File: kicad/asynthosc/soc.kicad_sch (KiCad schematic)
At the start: 50 parts, among them J15 Conn_02x04_Odd_Even, J3 Conn_ARM_SWD_TagConnect_TC203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, J4 Conn_02x07_Odd_Even, J5 Conn_02x04_Odd_Even, SW1 SW_Push, U6 STM32F723VETx, U7 W25Q32JVSS, Y1 8MHz, 8pF

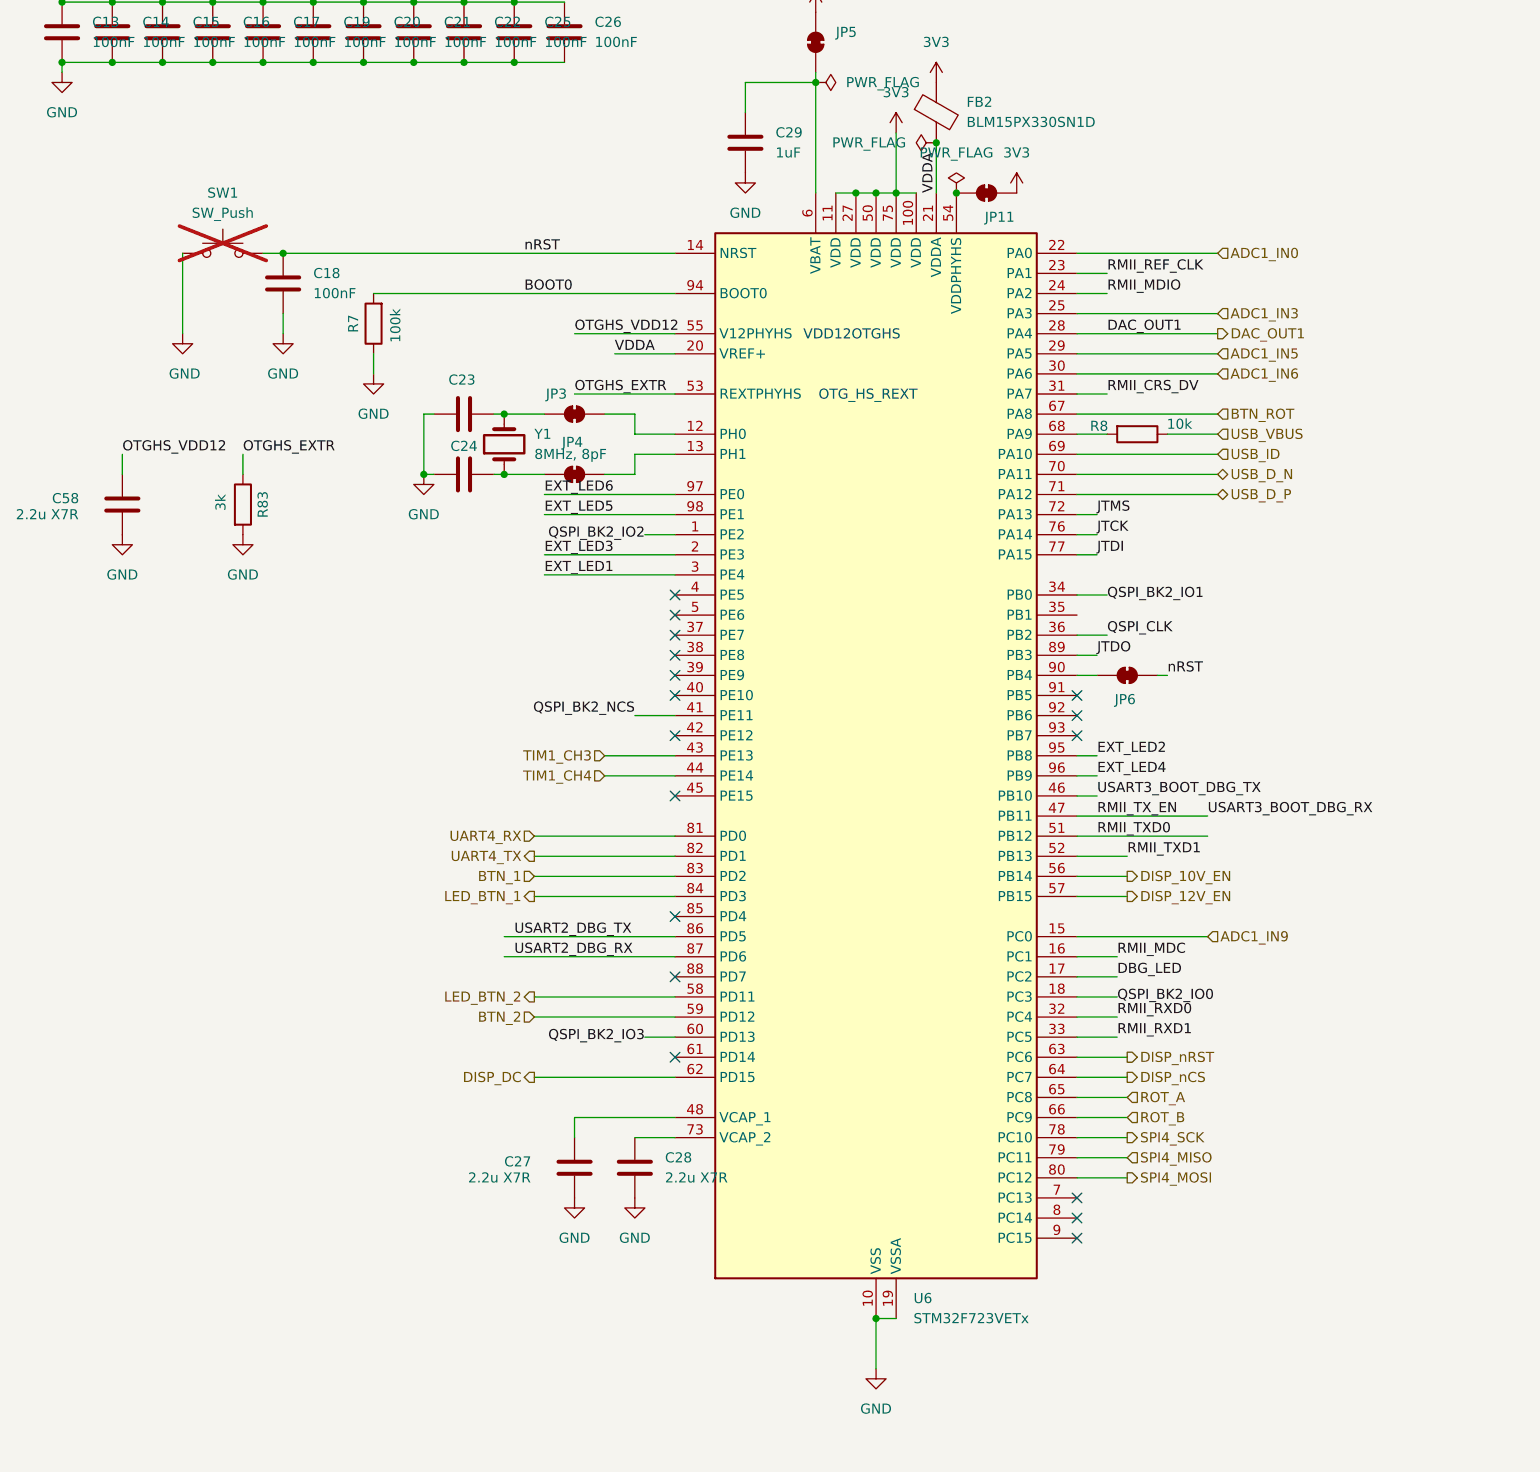
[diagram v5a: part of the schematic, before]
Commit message: sch: change stm32 ref for adc
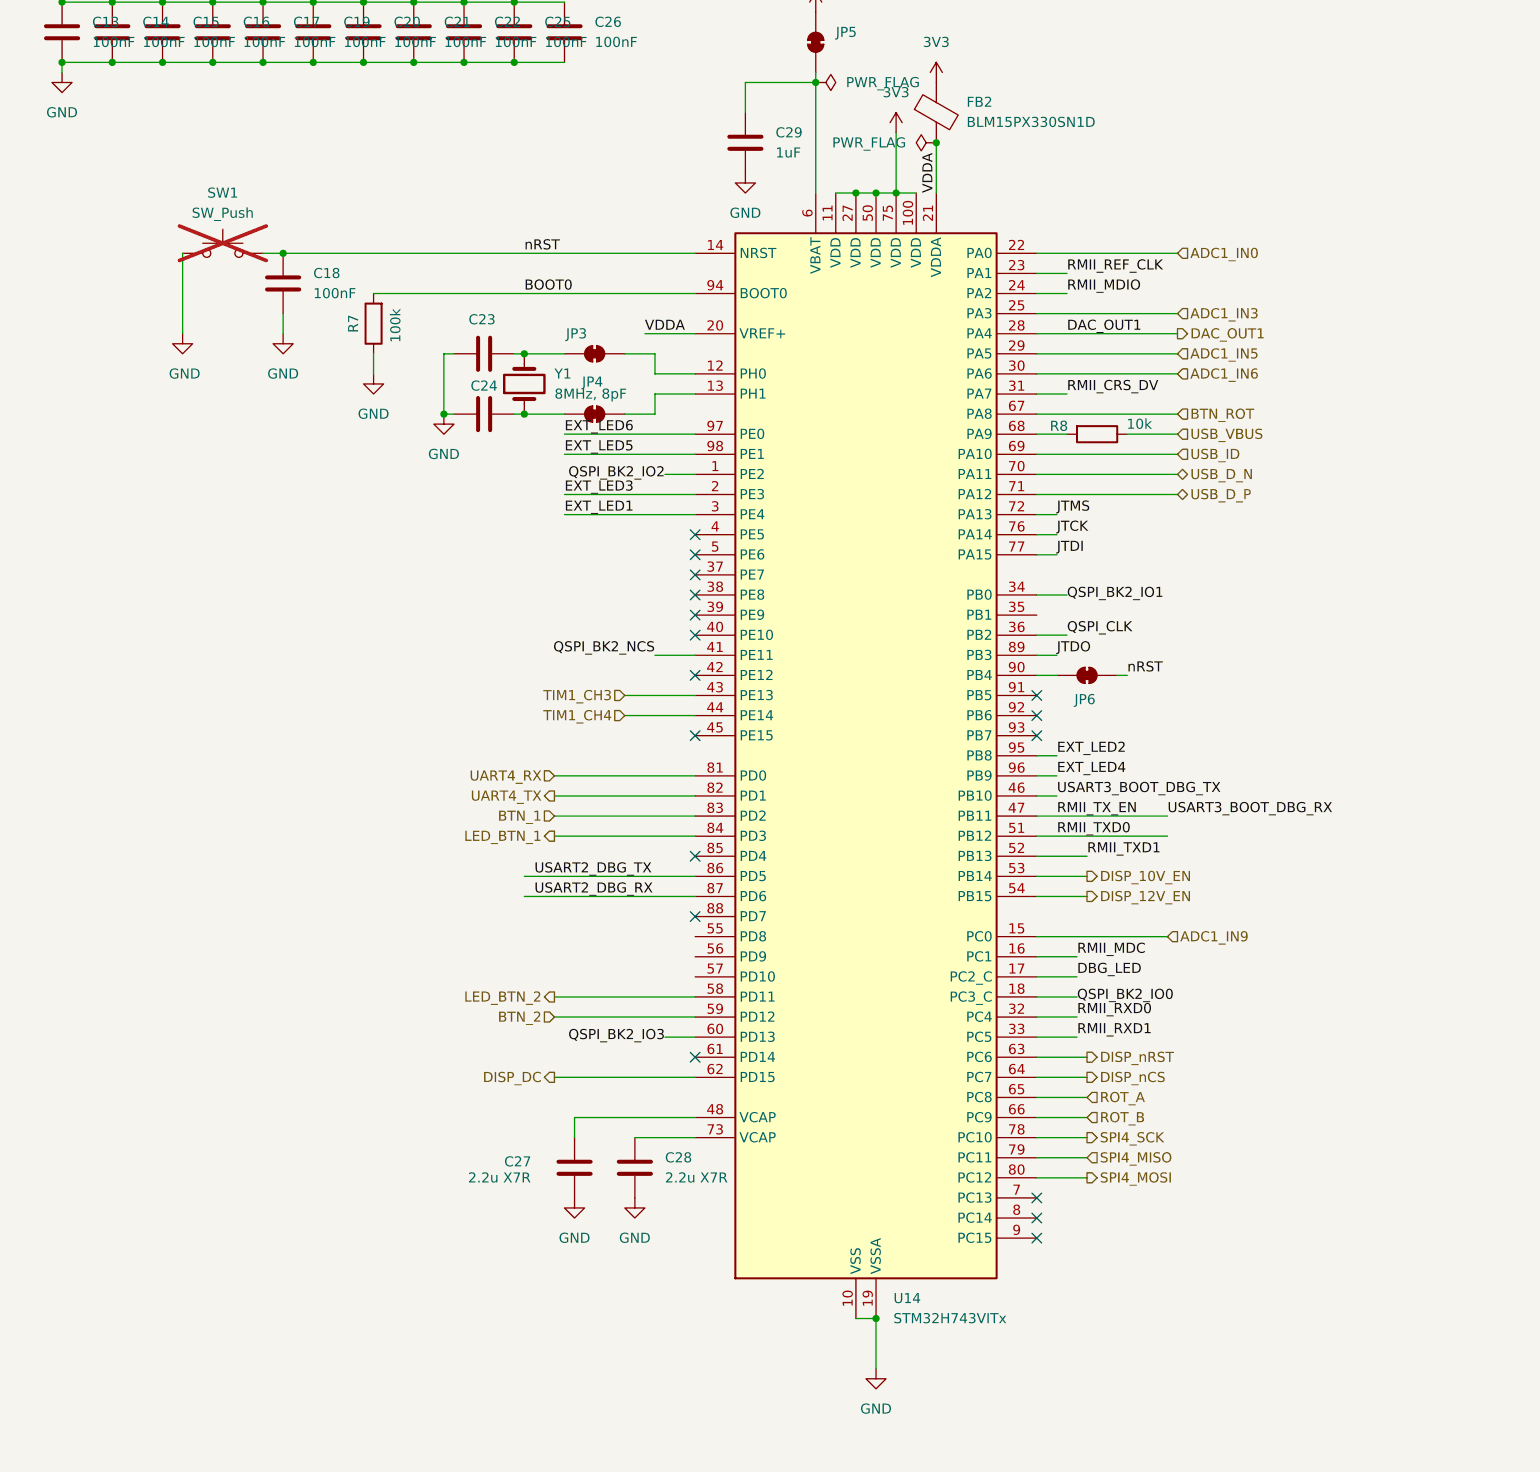
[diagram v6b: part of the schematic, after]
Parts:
- removed C58: 2.2u X7R, Capacitor_SMD:C_0402_1005Metric, symbol Device:C
- removed JP11: SolderJumper_2_Bridged, asynthosc:SolderJumper_0402_1005Metric_Bridged, symbol Jumper:SolderJumper_2_Bridged
- removed R83: 3k, Resistor_SMD:R_0402_1005Metric, symbol Device:R
- removed U6: STM32F723VETx, Package_QFP:LQFP-100_14x14mm_P0.5mm, symbol MCU_ST_STM32F7:STM32F723VETx
- added U14: STM32H743VITx, Package_QFP:LQFP-100_14x14mm_P0.5mm, symbol MCU_ST_STM32H7:STM32H743VITx
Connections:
- net 3V3: now also U14.100 (VDD), U14.11 (VDD), U14.27 (VDD), U14.50 (VDD), U14.75 (VDD)
- net ADC1_IN0: now also U14.22 (PA0)
- net ADC1_IN3: now also U14.25 (PA3)
- net ADC1_IN5: now also U14.29 (PA5)
- net ADC1_IN6: now also U14.30 (PA6)
- net ADC1_IN9: now also U14.15 (PC0)
- net BOOT0: now also U14.94 (BOOT0)
- net BTN_1: now also U14.83 (PD2)
- net BTN_2: now also U14.59 (PD12)
- net BTN_ROT: now also U14.67 (PA8)
- net DAC_OUT1: now also U14.28 (PA4)
- net DBG_LED: now also U14.17 (PC2_C)
- net DISP_10V_EN: now also U14.53 (PB14)
- net DISP_12V_EN: now also U14.54 (PB15)
- net DISP_DC: now also U14.62 (PD15)
- net DISP_nCS: now also U14.64 (PC7)
- net DISP_nRST: now also U14.63 (PC6)
- net EXT_LED1: now also U14.3 (PE4)
- net EXT_LED2: now also U14.95 (PB8)
- net EXT_LED3: now also U14.2 (PE3)
- net EXT_LED4: now also U14.96 (PB9)
- net EXT_LED5: now also U14.98 (PE1)
- net EXT_LED6: now also U14.97 (PE0)
- net GND: now also U14.10 (VSS), U14.19 (VSSA), U14.26 (VSS), U14.49 (VSS), U14.74 (VSS), U14.99 (VSS)
- net JTCK: now also U14.76 (PA14)
- net JTDI: now also U14.77 (PA15)
- net JTDO: now also U14.89 (PB3)
- net JTMS: now also U14.72 (PA13)
- net LED_BTN_1: now also U14.84 (PD3)
- net LED_BTN_2: now also U14.58 (PD11)
- net QSPI_BK2_IO0: now also U14.18 (PC3_C)
- net QSPI_BK2_IO1: now also U14.34 (PB0)
- net QSPI_BK2_IO2: now also U14.1 (PE2)
- net QSPI_BK2_IO3: now also U14.60 (PD13)
- net QSPI_BK2_NCS: now also U14.41 (PE11)
- net QSPI_CLK: now also U14.36 (PB2)
- net RMII_CRS_DV: now also U14.31 (PA7)
- net RMII_MDC: now also U14.16 (PC1)
- net RMII_MDIO: now also U14.24 (PA2)
- net RMII_REF_CLK: now also U14.23 (PA1)
- net RMII_RXD0: now also U14.32 (PC4)
- net RMII_RXD1: now also U14.33 (PC5)
- net RMII_TXD0: now also U14.51 (PB12)
- net RMII_TXD1: now also U14.52 (PB13)
- net RMII_TX_EN: now also U14.47 (PB11)
- net ROT_A: now also U14.65 (PC8)
- net ROT_B: now also U14.66 (PC9)
- net SPI4_MISO: now also U14.79 (PC11)
- net SPI4_MOSI: now also U14.80 (PC12)
- net SPI4_SCK: now also U14.78 (PC10)
- net TIM1_CH3: now also U14.43 (PE13)
- net TIM1_CH4: now also U14.44 (PE14)
- net UART4_RX: now also U14.81 (PD0)
- net UART4_TX: now also U14.82 (PD1)
- net USART2_DBG_RX: now also U14.87 (PD6)
- net USART2_DBG_TX: now also U14.86 (PD5)
- net USART3_BOOT_DBG_TX: now also U14.46 (PB10)
- net USB_D_N: now also U14.70 (PA11)
- net USB_D_P: now also U14.71 (PA12)
- net USB_ID: now also U14.69 (PA10)
- net VDDA: now also U14.20 (VREF+), U14.21 (VDDA)
- net nRST: now also U14.14 (NRST)
- net at JP4.1 (A): now also U14.13 (PH1)
- net at JP3.1 (A): now also U14.12 (PH0)
- net at C29.1, JP5.1 (A): now also U14.6 (VBAT)
- net at C27.1: now also U14.48 (VCAP)
- net at R8.2: now also U14.68 (PA9)
- net at C28.1: now also U14.73 (VCAP)
- net at JP6.2 (B): now also U14.90 (PB4)
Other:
- note removed: "OTG_HS_REXT"
- note removed: "VDD12OTGHS"
- moved on the sheet: C23, C24, JP3, JP4, JP6, R8, Y1

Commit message: bom: update mfr, serials and lcsc fields
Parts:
- FB2: LCSC (none) -> C160974
- J15, J5: LCSC (none) -> C192300; Manufacturer (none) -> Boomele; RefNum _na_ -> 2.54-2*4P
- J4: LCSC (none) -> C84004; Manufacturer (none) -> Boomele; RefNum _na_ -> 2.54-2*7P
- SW1: LCSC (none) -> C5127964; Manufacturer Boomele -> Boomele
- U14: LCSC (none) -> C114409; Manufacturer (none) -> STMicroelectronics; RefNum (none) -> STM32H743VITx
- U7: LCSC (none) -> C179173
- Y1: LCSC (none) -> C889706
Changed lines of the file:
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@@
 			)
 		)
-		(property "LCSC" ""
+		(property "LCSC" "C192300 "
 			(at 328.93 166.37 0)
 			(effects
@@
 			)
 		)
-		(property "Manufacturer" ""
+		(property "Manufacturer" "Boomele "
 			(at 328.93 166.37 0)
 			(effects
@@
 			)
 		)
-		(property "RefNum" "_na_"
+		(property "RefNum" "2.54-2*4P"
 			(at 328.93 166.37 0)
 			(effects
@@
 			)
 		)
-		(property "LCSC" ""
+		(property "LCSC" "C84004 "
 			(at 326.39 86.36 0)
 			(effects
@@
 			)
 		)
-		(property "Manufacturer" ""
+		(property "Manufacturer" "Boomele "
 			(at 326.39 86.36 0)
 			(effects
@@
 			)
 		)
-		(property "RefNum" "_na_"
+		(property "RefNum" "2.54-2*7P"
 			(at 326.39 86.36 0)
 			(effects
@@
 			)
 		)
-		(property "LCSC" ""
+		(property "LCSC" "C192300 "
 			(at 328.93 134.62 0)
 			(effects
@@
 			)
 		)
-		(property "Manufacturer" ""
+		(property "Manufacturer" "Boomele "
 			(at 328.93 134.62 0)
 			(effects
@@
 			)
 		)
-		(property "RefNum" "_na_"
+		(property "RefNum" "2.54-2*4P"
 			(at 328.93 134.62 0)
 			(effects
@@
 			)
 		)
-		(property "LCSC" ""
+		(property "LCSC" "C179173"
 			(at 278.13 218.44 0)
 			(effects
@@
 			)
 		)
+		(property "LCSC" " C114409"
+			(at 124.46 115.57 0)
+			(effects
+				(font
+					(size 1.27 1.27)
+				)
+				(hide yes)
+			)
+		)
+		(property "Manufacturer" "STMicroelectronics"
+			(at 124.46 115.57 0)
+			(effects
+				(font
+					(size 1.27 1.27)
+				)
+				(hide yes)
+			)
+		)
+		(property "RefNum" "STM32H743VITx"
+			(at 124.46 115.57 0)
+			(effects
+				(font
+					(size 1.27 1.27)
+				)
+				(hide yes)
+			)
+		)
 		(pin "86"
 		)
@@
 			)
 		)
-		(property "LCSC" ""
+		(property "LCSC" "C889706"
 			(at 82.55 68.58 0)
 			(effects
@@
 			)
 		)
-		(property "LCSC" ""
+		(property "LCSC" "C160974"
 			(at 134.62 34.29 0)
 			(effects
@@
 			)
 		)
-		(property "LCSC" ""
+		(property "LCSC" "C5127964"
 			(at 44.45 52.07 0)
 			(effects
@@
 			)
 		)
-		(property "Manufacturer" " Boomele"
+		(property "Manufacturer" "Boomele"
 			(at 44.45 52.07 0)
 			(effects

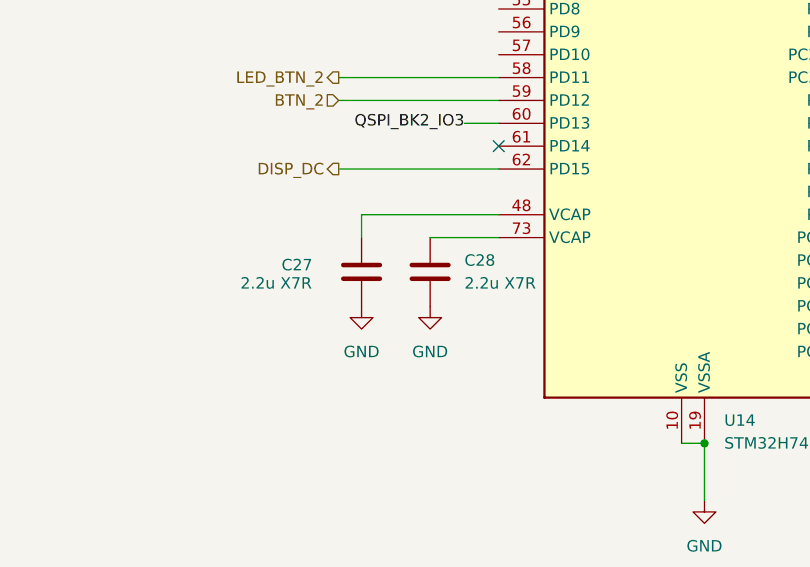
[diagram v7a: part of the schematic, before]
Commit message: bom: update for better bom
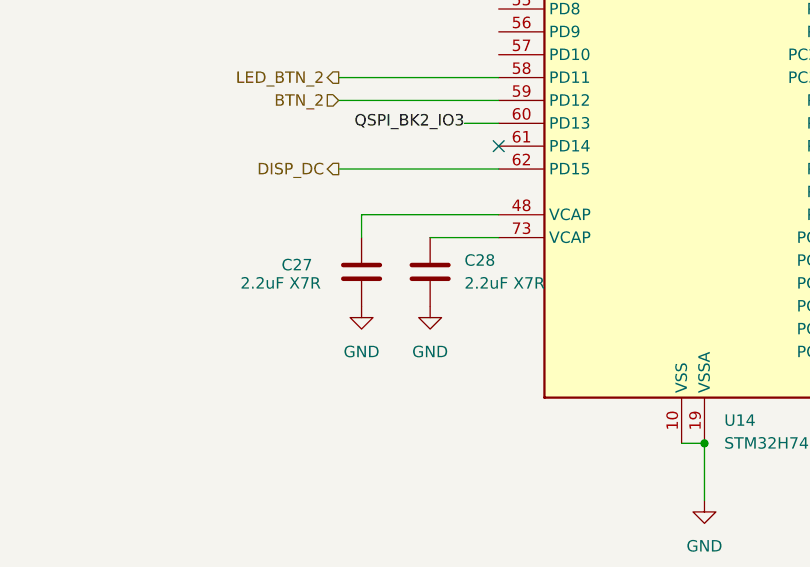
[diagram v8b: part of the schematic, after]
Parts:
- C27, C28: value 2.2u X7R -> 2.2uF X7R
- D7, D8: footprint LED_SMD:LED_0402_1005Metric -> LED_SMD:LED_0805_2012Metric
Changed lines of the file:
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@@
 			)
 		)
-		(property "Footprint" "LED_SMD:LED_0402_1005Metric"
+		(property "Footprint" "LED_SMD:LED_0805_2012Metric"
 			(at 237.49 53.34 0)
 			(effects
@@
 			)
 		)
-		(property "Value" "2.2u X7R"
+		(property "Value" "2.2uF X7R"
 			(at 100.33 168.9099 0)
 			(effects
@@
 			)
 		)
-		(property "Footprint" "LED_SMD:LED_0402_1005Metric"
+		(property "Footprint" "LED_SMD:LED_0805_2012Metric"
 			(at 251.46 53.34 0)
 			(effects
@@
 			)
 		)
-		(property "Value" "2.2u X7R"
+		(property "Value" "2.2uF X7R"
 			(at 75.438 168.91 0)
 			(effects
